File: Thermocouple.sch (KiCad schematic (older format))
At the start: 28 parts, among them P2 CONN_2, P3 CONN_3X2, U10 LMT84, U11 OPA4170, U9 MCP3901

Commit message: Added some R/C to analog sections
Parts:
- added R62, R64: 1k, symbol R
- added R63: 0, symbol R
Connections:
- net AGND: now also R62.2, R63.1; no longer C31.2, R22.1, R48.1, U9.10 (REFIN-)
- net CH1+: now also R62.1, R64.1; no longer U10.3 (OUT)
- net TC_IN+: now also U11.12 (+); no longer U11.10 (+)
- net TC_IN-: now also U11.10 (+); no longer U11.12 (+)
- new net: R22.1, R48.1, R63.2
- new net: C31.2, U9.10 (REFIN-)
- new net: R64.2, U10.3 (OUT)
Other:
- moved on the sheet: C10, U10
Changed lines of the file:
@@
 $EndDescr
 Text HLabel 9000 1800 2    60   Input ~ 0
+TC_IN-
+Text HLabel 9000 4350 2    60   Input ~ 0
 TC_IN+
-Text HLabel 9000 4350 2    60   Input ~ 0
-TC_IN-
 Text HLabel 1050 2850 0    60   Input ~ 0
 MOSI
@@
 L LMT84 U10
 U 1 1 53054140
-P 5050 5600
-F 0 "U10" H 5300 5150 60  0000 C CNN
-F 1 "LMT84" H 5250 5600 60  0000 C CNN
-F 2 "" H 5050 5600 60  0000 C CNN
-F 3 "" H 5050 5600 60  0000 C CNN
-	1    5050 5600
+P 6300 5600
+F 0 "U10" H 6550 5150 60  0000 C CNN
+F 1 "LMT84" H 6500 5600 60  0000 C CNN
+F 2 "" H 6300 5600 60  0000 C CNN
+F 3 "" H 6300 5600 60  0000 C CNN
+	1    6300 5600
 	1    0    0    -1
 $EndComp
@@
 L +5V #PWR047
 U 1 1 530546E7
-P 5050 4750
-F 0 "#PWR047" H 5050 4840 20  0001 C CNN
-F 1 "+5V" H 5050 4840 30  0000 C CNN
-F 2 "" H 5050 4750 60  0000 C CNN
-F 3 "" H 5050 4750 60  0000 C CNN
-	1    5050 4750
+P 6300 4750
+F 0 "#PWR047" H 6300 4840 20  0001 C CNN
+F 1 "+5V" H 6300 4840 30  0000 C CNN
+F 2 "" H 6300 4750 60  0000 C CNN
+F 3 "" H 6300 4750 60  0000 C CNN
+	1    6300 4750
 	1    0    0    -1
 $EndComp
@@
 L C C10
 U 1 1 53054751
-P 5700 5550
-F 0 "C10" H 5700 5650 40  0000 L CNN
-F 1 "C" H 5706 5465 40  0000 L CNN
-F 2 "" H 5738 5400 30  0000 C CNN
-F 3 "" H 5700 5550 60  0000 C CNN
-	1    5700 5550
+P 6950 5550
+F 0 "C10" H 6950 5650 40  0000 L CNN
+F 1 "C" H 6956 5465 40  0000 L CNN
+F 2 "" H 6988 5400 30  0000 C CNN
+F 3 "" H 6950 5550 60  0000 C CNN
+	1    6950 5550
 	1    0    0    -1
 $EndComp
@@
 	0    -1   -1   0
 $EndComp
-Text Notes 5900 5550 0    60   ~ 0
+Text Notes 7150 5550 0    60   ~ 0
 Temperature Sensor
 Text Notes 3450 2000 0    60   ~ 0
@@
 $EndComp
 $Comp
-L FE_V- #PWR64
+L FE_V- #PWR63
 U 1 1 530BD604
 P 5300 2400
-F 0 "#PWR64" H 5300 2600 40  0001 C CNN
+F 0 "#PWR63" H 5300 2600 40  0001 C CNN
 F 1 "FE_V-" H 5300 2550 30  0000 C CNN
 F 2 "" H 5300 2400 60  0000 C CNN
@@
 L AGND #PWR059
 U 1 1 531E51B9
-P 4500 4450
-F 0 "#PWR059" H 4500 4450 40  0001 C CNN
-F 1 "AGND" H 4500 4380 50  0000 C CNN
-F 2 "" H 4500 4450 60  0000 C CNN
-F 3 "" H 4500 4450 60  0000 C CNN
-	1    4500 4450
+P 4500 5000
+F 0 "#PWR059" H 4500 5000 40  0001 C CNN
+F 1 "AGND" H 4500 4930 50  0000 C CNN
+F 2 "" H 4500 5000 60  0000 C CNN
+F 3 "" H 4500 5000 60  0000 C CNN
+	1    4500 5000
 	1    0    0    -1
 $EndComp
@@
 	-1   0    0    -1
 $EndComp
-$Comp
-L AGND #PWR060
-U 1 1 5320CB7D
-P 3950 2600
-F 0 "#PWR060" H 3950 2600 40  0001 C CNN
-F 1 "AGND" H 3950 2530 50  0000 C CNN
-F 2 "" H 3950 2600 60  0000 C CNN
-F 3 "" H 3950 2600 60  0000 C CNN
-	1    3950 2600
-	1    0    0    -1
-$EndComp
-Connection ~ 3950 2500
-Wire Wire Line
-	3950 2350 3950 2600
 Wire Wire Line
 	3950 2100 3950 2250
@@
 	3950 3550 4200 3550
 Wire Wire Line
-	4200 6300 5700 6300
-Wire Wire Line
-	4950 6300 4950 6200
-Wire Wire Line
-	5050 6300 5050 6200
-Connection ~ 4950 6300
-Wire Wire Line
-	5150 6300 5150 6200
-Connection ~ 5050 6300
+	4200 6300 6950 6300
+Wire Wire Line
+	6200 6300 6200 6200
+Wire Wire Line
+	6300 6300 6300 6200
+Connection ~ 6200 6300
+Wire Wire Line
+	6400 6300 6400 6200
+Connection ~ 6300 6300
 Wire Wire Line
 	3950 3450 4300 3450
@@
 	4300 3250 4300 5600
 Wire Wire Line
-	4300 5600 4500 5600
-Wire Wire Line
-	5050 4750 5050 5000
-Wire Wire Line
-	5050 4900 5700 4900
-Wire Wire Line
-	5700 4900 5700 5350
-Connection ~ 5050 4900
-Wire Wire Line
-	5700 6300 5700 5750
-Connection ~ 5150 6300
+	6300 4750 6300 5000
+Wire Wire Line
+	6300 4900 6950 4900
+Wire Wire Line
+	6950 4900 6950 5350
+Connection ~ 6300 4900
+Wire Wire Line
+	6950 6300 6950 5750
+Connection ~ 6400 6300
 Wire Wire Line
 	4800 2450 4800 2550
@@
 	4500 3100 4500 3700
 Wire Wire Line
-	4500 4200 4500 4450
+	4500 4200 4500 4300
+Wire Wire Line
+	4500 4800 4500 5000
 Connection ~ 5900 4250
 Wire Wire Line
@@
 	3250 1350 3100 1350
 Connection ~ 3100 1350
+$Comp
+L R R63
+U 1 1 53236D2C
+P 4500 4550
+F 0 "R63" V 4580 4550 40  0000 C CNN
+F 1 "0" V 4507 4551 40  0000 C CNN
+F 2 "" V 4430 4550 30  0000 C CNN
+F 3 "" H 4500 4550 30  0000 C CNN
+	1    4500 4550
+	-1   0    0    1
+$EndComp
+$Comp
+L R R64
+U 1 1 53236DD2
+P 4800 5600
+F 0 "R64" V 4880 5600 40  0000 C CNN
+F 1 "1k" V 4807 5601 40  0000 C CNN
+F 2 "" V 4730 5600 30  0000 C CNN
+F 3 "" H 4800 5600 30  0000 C CNN
+	1    4800 5600
+	0    -1   -1   0
+$EndComp
+Wire Wire Line
+	4300 5600 4550 5600
+Wire Wire Line
+	5050 5600 5750 5600
+$Comp
+L R R62
+U 1 1 53236ED8
+P 4450 5950
+F 0 "R62" V 4530 5950 40  0000 C CNN
+F 1 "1k" V 4457 5951 40  0000 C CNN
+F 2 "" V 4380 5950 30  0000 C CNN
+F 3 "" H 4450 5950 30  0000 C CNN
+	1    4450 5950
+	1    0    0    -1
+$EndComp
+Wire Wire Line
+	4450 5700 4450 5600
+Connection ~ 4450 5600
+Wire Wire Line
+	4450 6200 4450 6300
+Connection ~ 4450 6300
+Wire Wire Line
+	3950 2500 3950 2350
 $EndSCHEMATC

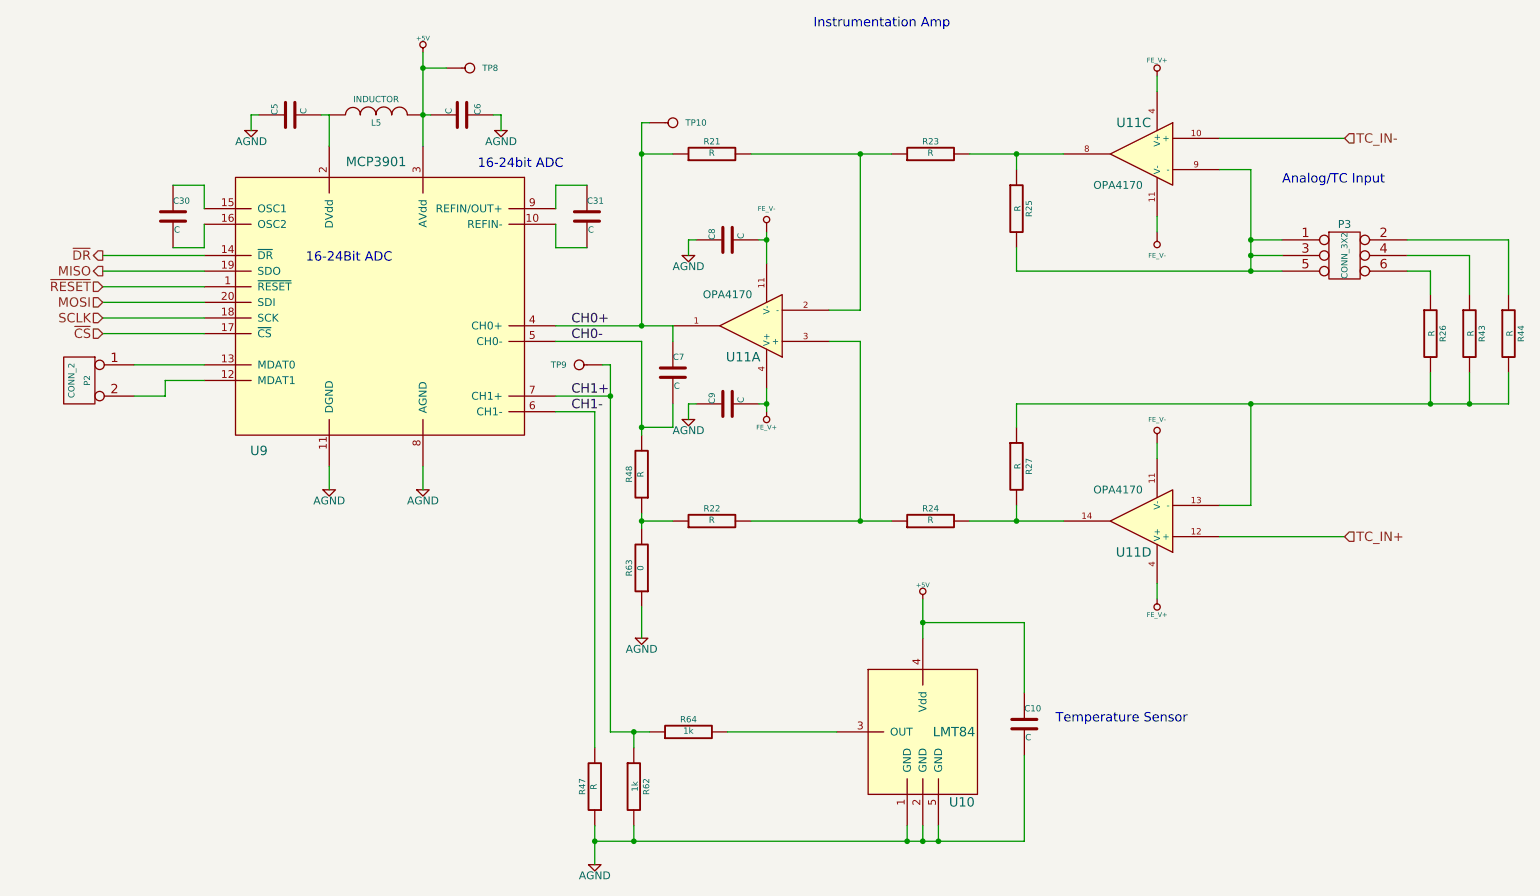
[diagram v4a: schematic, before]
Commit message: Assigned values to passives in fan and thermocouple schematics
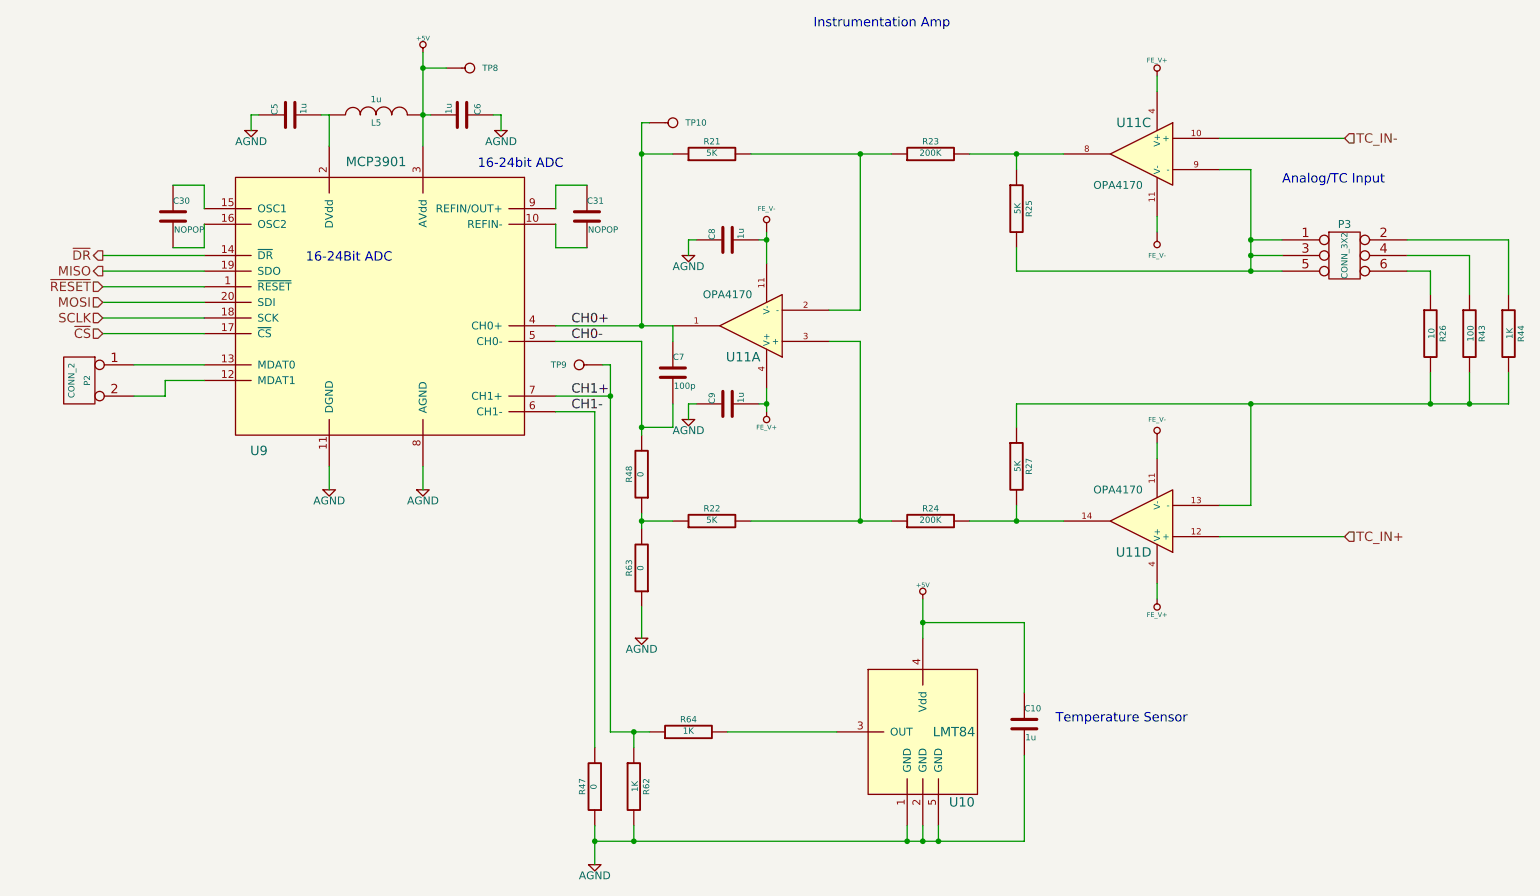
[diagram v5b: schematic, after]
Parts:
- C10, C5, C6, C8, C9: value C -> 1u
- C30, C31: value C -> NOPOP
- C7: value C -> 100p
- L5: value INDUCTOR -> 1u
- R21, R22, R25, R27: value R -> 5K
- R23, R24: value R -> 200K
- R26: value R -> 10
- R43: value R -> 100
- R44: value R -> 1K
- R47, R48: value R -> 0
- R62, R64: value 1k -> 1K
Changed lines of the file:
@@
 P 6900 2250
 F 0 "R25" V 6980 2250 40  0000 C CNN
-F 1 "R" V 6907 2251 40  0000 C CNN
+F 1 "5K" V 6907 2251 40  0000 C CNN
 F 2 "" V 6830 2250 30  0000 C CNN
 F 3 "" H 6900 2250 30  0000 C CNN
@@
 P 6900 3900
 F 0 "R27" V 6980 3900 40  0000 C CNN
-F 1 "R" V 6907 3901 40  0000 C CNN
+F 1 "5K" V 6907 3901 40  0000 C CNN
 F 2 "" V 6830 3900 30  0000 C CNN
 F 3 "" H 6900 3900 30  0000 C CNN
@@
 P 6350 1900
 F 0 "R23" V 6430 1900 40  0000 C CNN
-F 1 "R" V 6357 1901 40  0000 C CNN
+F 1 "200K" V 6357 1901 40  0000 C CNN
 F 2 "" V 6280 1900 30  0000 C CNN
 F 3 "" H 6350 1900 30  0000 C CNN
@@
 P 4950 1900
 F 0 "R21" V 5030 1900 40  0000 C CNN
-F 1 "R" V 4957 1901 40  0000 C CNN
+F 1 "5K" V 4957 1901 40  0000 C CNN
 F 2 "" V 4880 1900 30  0000 C CNN
 F 3 "" H 4950 1900 30  0000 C CNN
@@
 P 6350 4250
 F 0 "R24" V 6430 4250 40  0000 C CNN
-F 1 "R" V 6357 4251 40  0000 C CNN
+F 1 "200K" V 6357 4251 40  0000 C CNN
 F 2 "" V 6280 4250 30  0000 C CNN
 F 3 "" H 6350 4250 30  0000 C CNN
@@
 P 4950 4250
 F 0 "R22" V 5030 4250 40  0000 C CNN
-F 1 "R" V 4957 4251 40  0000 C CNN
+F 1 "5K" V 4957 4251 40  0000 C CNN
 F 2 "" V 4880 4250 30  0000 C CNN
 F 3 "" H 4950 4250 30  0000 C CNN
@@
 P 4700 3300
 F 0 "C7" H 4700 3400 40  0000 L CNN
-F 1 "C" H 4706 3215 40  0000 L CNN
+F 1 "100p" H 4706 3215 40  0000 L CNN
 F 2 "" H 4738 3150 30  0000 C CNN
 F 3 "" H 4700 3300 60  0000 C CNN
@@
 P 9550 3050
 F 0 "R26" V 9630 3050 40  0000 C CNN
-F 1 "R" V 9557 3051 40  0000 C CNN
+F 1 "10" V 9557 3051 40  0000 C CNN
 F 2 "" V 9480 3050 30  0000 C CNN
 F 3 "" H 9550 3050 30  0000 C CNN
@@
 P 9800 3050
 F 0 "R43" V 9880 3050 40  0000 C CNN
-F 1 "R" V 9807 3051 40  0000 C CNN
+F 1 "100" V 9807 3051 40  0000 C CNN
 F 2 "" V 9730 3050 30  0000 C CNN
 F 3 "" H 9800 3050 30  0000 C CNN
@@
 P 10050 3050
 F 0 "R44" V 10130 3050 40  0000 C CNN
-F 1 "R" V 10057 3051 40  0000 C CNN
+F 1 "1K" V 10057 3051 40  0000 C CNN
 F 2 "" V 9980 3050 30  0000 C CNN
 F 3 "" H 10050 3050 30  0000 C CNN
@@
 P 6950 5550
 F 0 "C10" H 6950 5650 40  0000 L CNN
-F 1 "C" H 6956 5465 40  0000 L CNN
+F 1 "1u" H 6956 5465 40  0000 L CNN
 F 2 "" H 6988 5400 30  0000 C CNN
 F 3 "" H 6950 5550 60  0000 C CNN
@@
 P 5050 2450
 F 0 "C8" H 5050 2550 40  0000 L CNN
-F 1 "C" H 5056 2365 40  0000 L CNN
+F 1 "1u" H 5056 2365 40  0000 L CNN
 F 2 "" H 5088 2300 30  0000 C CNN
 F 3 "" H 5050 2450 60  0000 C CNN
@@
 P 5050 3500
 F 0 "C9" H 5050 3600 40  0000 L CNN
-F 1 "C" H 5056 3415 40  0000 L CNN
+F 1 "1u" H 5056 3415 40  0000 L CNN
 F 2 "" H 5088 3350 30  0000 C CNN
 F 3 "" H 5050 3500 60  0000 C CNN
@@
 P 3350 1650
 F 0 "C6" H 3350 1750 40  0000 L CNN
-F 1 "C" H 3356 1565 40  0000 L CNN
+F 1 "1u" H 3356 1565 40  0000 L CNN
 F 2 "" H 3388 1500 30  0000 C CNN
 F 3 "" H 3350 1650 60  0000 C CNN
@@
 P 2250 1650
 F 0 "C5" H 2250 1750 40  0000 L CNN
-F 1 "C" H 2256 1565 40  0000 L CNN
+F 1 "1u" H 2256 1565 40  0000 L CNN
 F 2 "" H 2288 1500 30  0000 C CNN
 F 3 "" H 2250 1650 60  0000 C CNN
@@
 P 4500 3950
 F 0 "R48" V 4580 3950 40  0000 C CNN
-F 1 "R" V 4507 3951 40  0000 C CNN
+F 1 "0" V 4507 3951 40  0000 C CNN
 F 2 "" V 4430 3950 30  0000 C CNN
 F 3 "" H 4500 3950 30  0000 C CNN
@@
 P 4200 5950
 F 0 "R47" V 4280 5950 40  0000 C CNN
-F 1 "R" V 4207 5951 40  0000 C CNN
+F 1 "0" V 4207 5951 40  0000 C CNN
 F 2 "" V 4130 5950 30  0000 C CNN
 F 3 "" H 4200 5950 30  0000 C CNN
@@
 P 2800 1650
 F 0 "L5" V 2750 1650 40  0000 C CNN
-F 1 "INDUCTOR" V 2900 1650 40  0000 C CNN
+F 1 "1u" V 2900 1650 40  0000 C CNN
 F 2 "" H 2800 1650 60  0000 C CNN
 F 3 "" H 2800 1650 60  0000 C CNN
@@
 P 1500 2300
 F 0 "C30" H 1500 2400 40  0000 L CNN
-F 1 "C" H 1506 2215 40  0000 L CNN
+F 1 "NOPOP" H 1506 2215 40  0000 L CNN
 F 2 "" H 1538 2150 30  0000 C CNN
 F 3 "" H 1500 2300 60  0000 C CNN
@@
 P 4150 2300
 F 0 "C31" H 4150 2400 40  0000 L CNN
-F 1 "C" H 4156 2215 40  0000 L CNN
+F 1 "NOPOP" H 4156 2215 40  0000 L CNN
 F 2 "" H 4188 2150 30  0000 C CNN
 F 3 "" H 4150 2300 60  0000 C CNN
@@
 P 4800 5600
 F 0 "R64" V 4880 5600 40  0000 C CNN
-F 1 "1k" V 4807 5601 40  0000 C CNN
+F 1 "1K" V 4807 5601 40  0000 C CNN
 F 2 "" V 4730 5600 30  0000 C CNN
 F 3 "" H 4800 5600 30  0000 C CNN
@@
 P 4450 5950
 F 0 "R62" V 4530 5950 40  0000 C CNN
-F 1 "1k" V 4457 5951 40  0000 C CNN
+F 1 "1K" V 4457 5951 40  0000 C CNN
 F 2 "" V 4380 5950 30  0000 C CNN
 F 3 "" H 4450 5950 30  0000 C CNN
